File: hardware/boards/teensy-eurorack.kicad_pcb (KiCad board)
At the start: 2 copper layers, 118.1 x 101.6 mm, 98 parts, among them J10 AudioJack3_SwitchTR, J27 Conn_01x02, J28 Conn_02x08_Odd_Even, J4 AudioJack3_SwitchTR, J5 AudioJack3_SwitchTR, J6 AudioJack3_SwitchTR, J7 AudioJack3_SwitchTR, J8 AudioJack3_SwitchTR, J9 AudioJack3_SwitchTR, U1 CS42448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

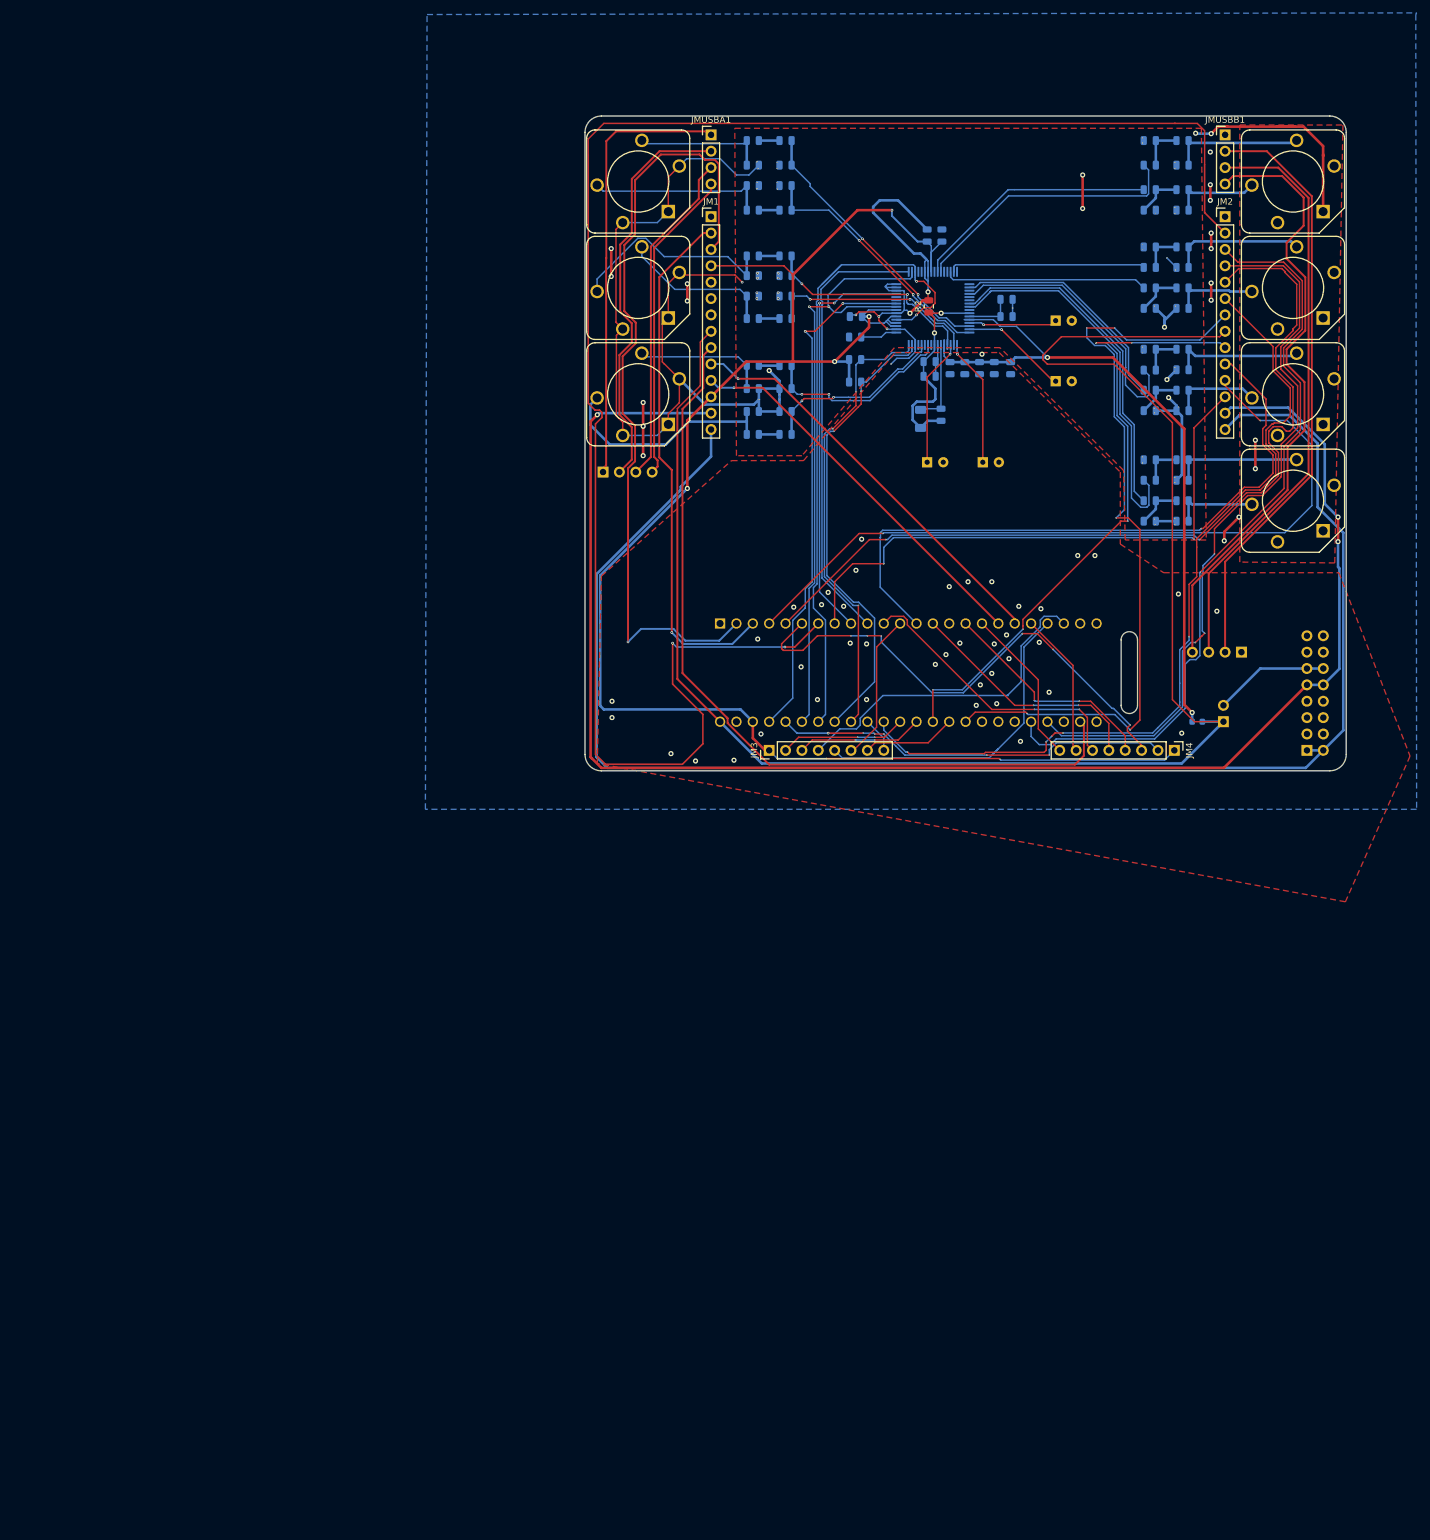
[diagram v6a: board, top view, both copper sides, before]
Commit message: repositioned board to middle of page
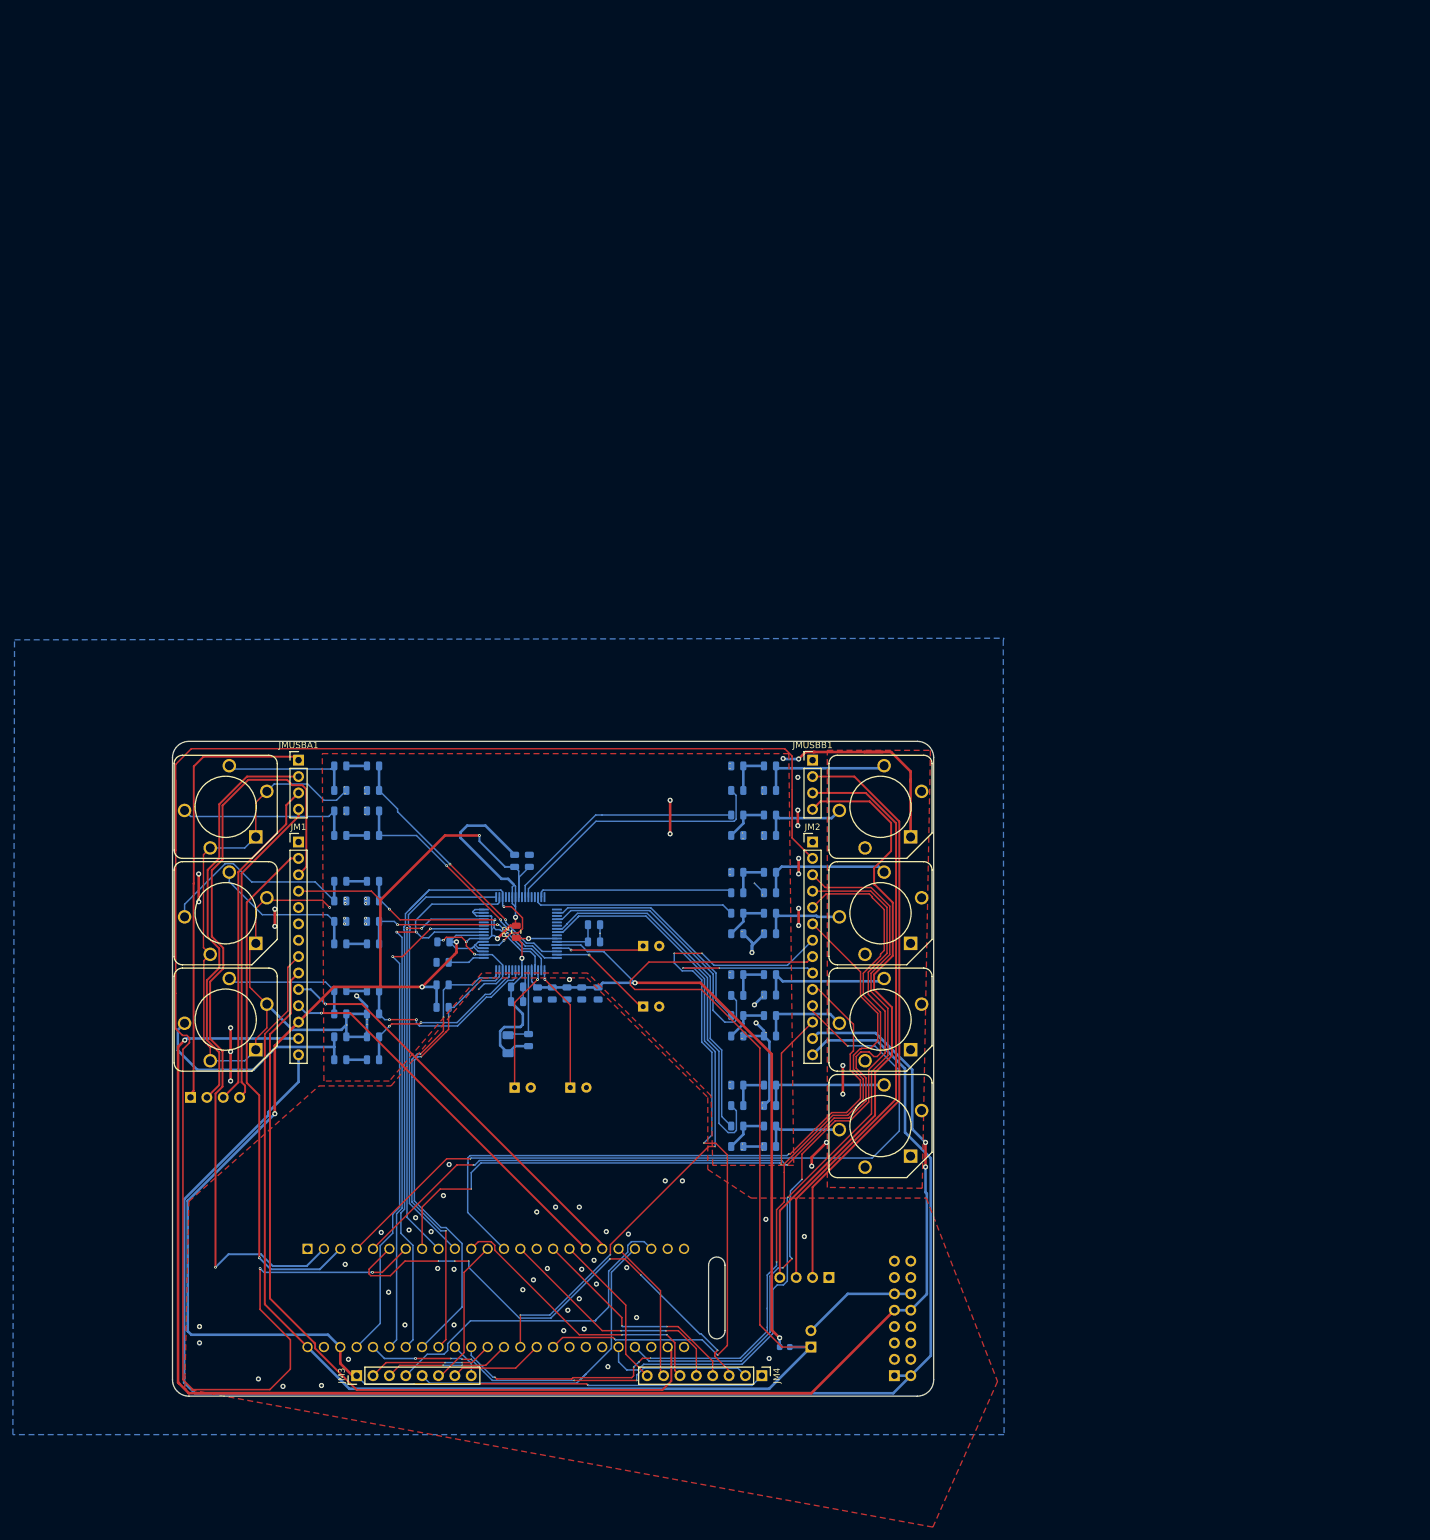
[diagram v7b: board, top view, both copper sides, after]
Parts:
- moved J28 116.2 mm to (201.7, 142.1)
- moved C1 116.2 mm to (162.7, 75.4)
- moved C10 116.2 mm to (146.3, 82.8)
- moved C11 116.2 mm to (153.2, 82.8)
- moved C14 116.2 mm to (143.1, 81.8)
- moved C15 116.2 mm to (143.1, 84.1)
- moved C16 116.2 mm to (141.7, 90.7)
- moved C17 116.2 mm to (144.9, 90.0)
- moved C18 116.2 mm to (155.7, 82.8)
- moved C3 116.2 mm to (151.4, 97.4)
- moved C4 116.2 mm to (142.7, 97.4)
- moved C45 116.2 mm to (177.3, 55.1)
- moved C46 116.2 mm to (177.3, 51.3)
- moved C49 116.2 mm to (177.3, 70.4)
- moved C50 116.2 mm to (177.3, 67.2)
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
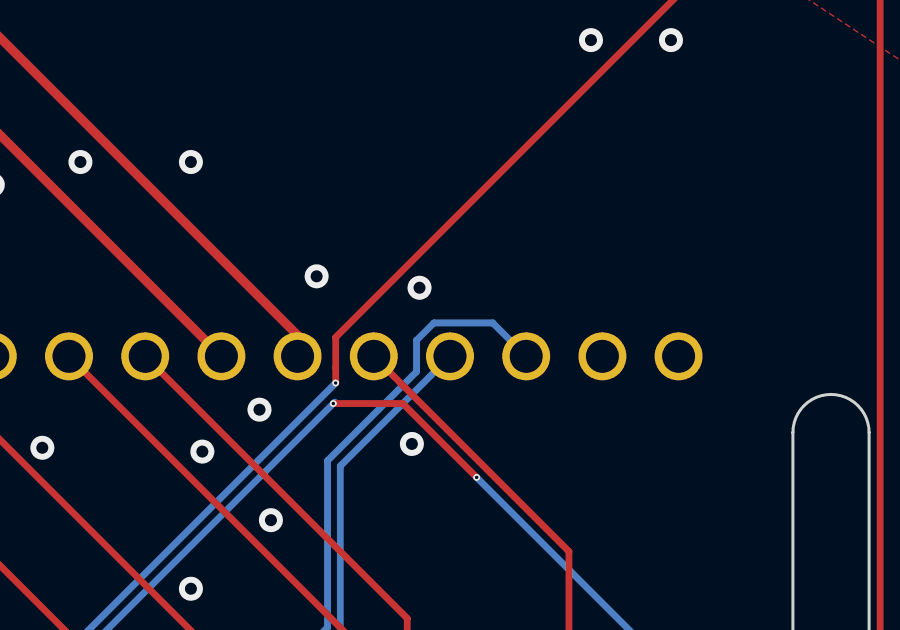
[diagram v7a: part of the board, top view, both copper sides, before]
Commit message: connected DAC_SCK output (pin 19) to pin 31, corrected audio out 4 AGND net (was disconnected)
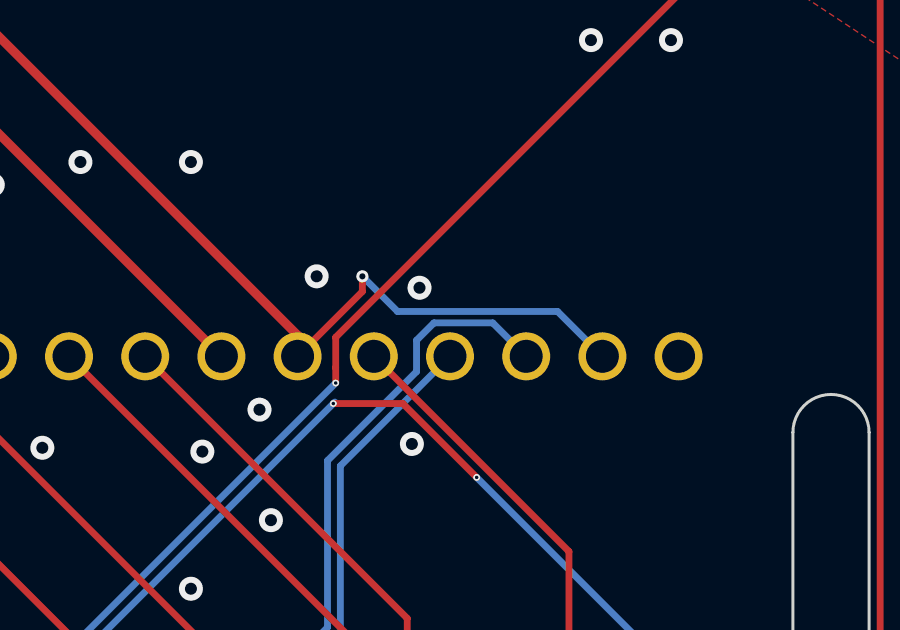
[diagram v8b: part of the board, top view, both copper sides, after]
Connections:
- U4 pad 23: Net-(U4-Pad23) -> /DAC_SCK
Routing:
- net /DAC_SCK: track 64.2 -> 76.9 mm, vias 1 -> 2
